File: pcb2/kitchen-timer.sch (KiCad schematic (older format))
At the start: 35 parts, among them IC1 TP4056, J1 BATT, J2 SW2, J3 RT, J4 LCD, J5 RTC, J6 USB IN, J7 Conn_01x02_Male, Q1 BC817, Q2 BC817, Q3 BC807, U1 ATmega328-PU, U2 FS8205A, U3 DW01A, Y1 32khz

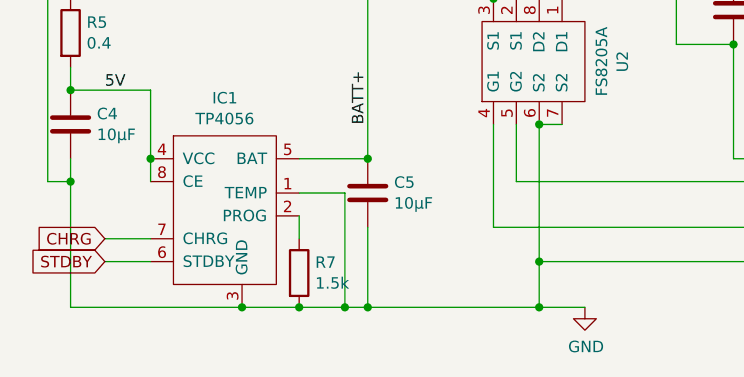
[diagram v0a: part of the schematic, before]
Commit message: update tp4056 charge load
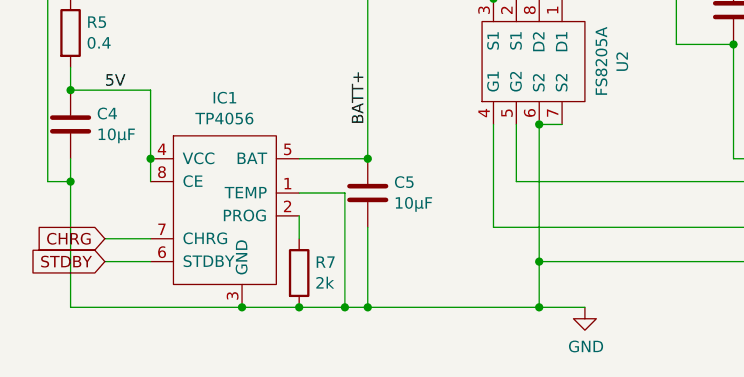
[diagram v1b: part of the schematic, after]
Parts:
- R7: value 1.5k -> 2k
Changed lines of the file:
@@
 P 1650 7400
 F 0 "R7" H 1720 7446 50  0000 L CNN
-F 1 "1.5k" H 1720 7355 50  0000 L CNN
+F 1 "2k" H 1720 7355 50  0000 L CNN
 F 2 "Resistor_SMD:R_0805_2012Metric" V 1580 7400 50  0001 C CNN
 F 3 "~" H 1650 7400 50  0001 C CNN
